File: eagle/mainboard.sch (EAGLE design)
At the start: 50 parts

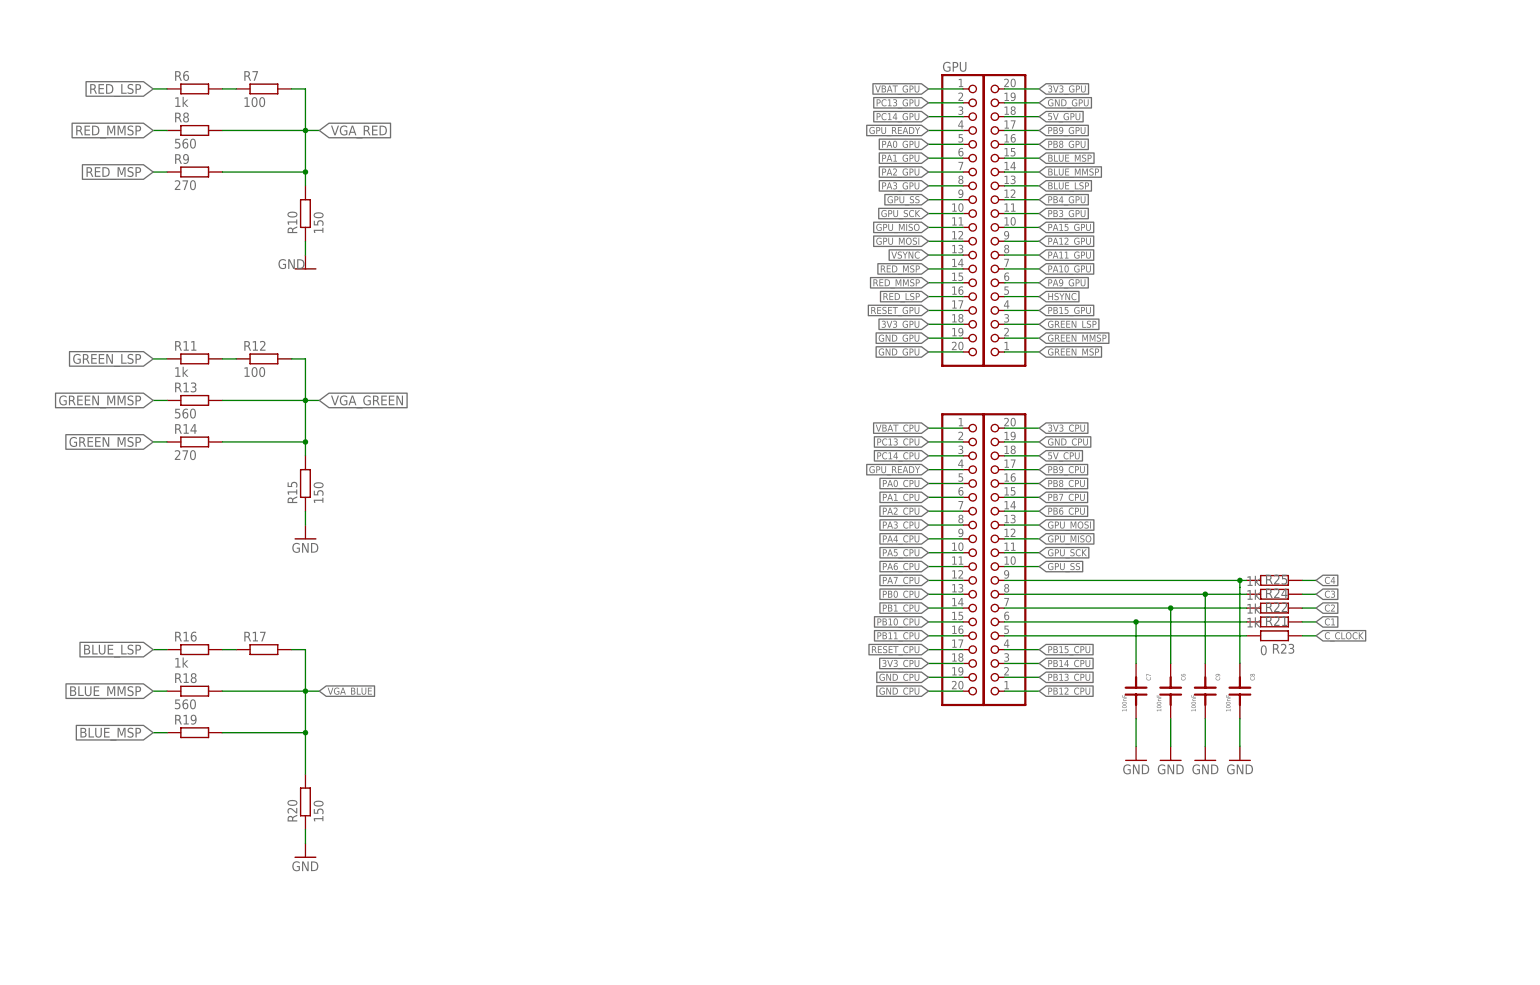
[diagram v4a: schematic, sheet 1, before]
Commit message: changed connector library ad wired up to cpu/gpu
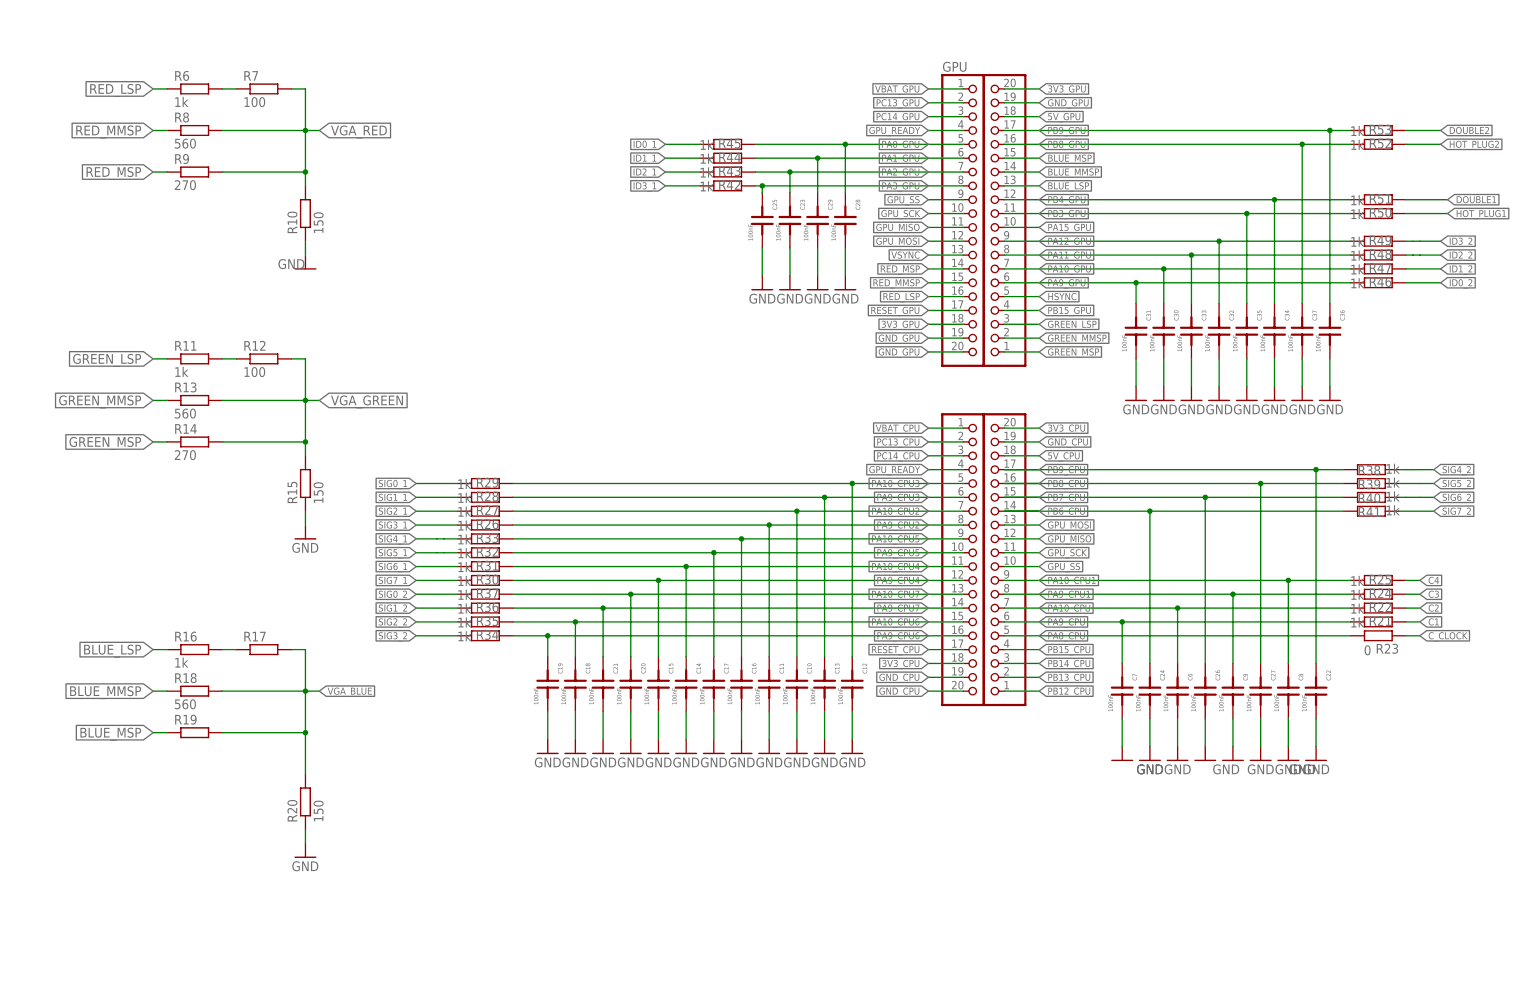
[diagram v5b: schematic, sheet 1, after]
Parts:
- added C10, C11, C12, C13, C14, C15, C16, C17, C18, C19, C20, C21, C22, C23, C24, C25, C26, C27, C28, C29, C30, C31, C32, C33, C34, C35, C36, C37: 100nF, deto:C1
- added R26, R27, R28, R29, R30, R31, R32, R33, R34, R35, R36, R37, R38, R39, R40, R41, R42, R43, R44, R45, R46, R47, R48, R49, R50, R51, R52, R53: 1k, rcl:R-EU_R0805
- added U$2: 3511220BMSS0BNA1_2.54MM_2X20_MALE, BtoB_connector:3511220BMSS0BNA1_2.54MM_2X20_MALE
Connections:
- removed net PA0_CPU: CPU2.5
- removed net PA1_CPU: CPU2.6
- removed net PA2_CPU: CPU2.7
- removed net PA3_CPU: CPU2.8
- removed net PA4_CPU: CPU2.9
- removed net PA5_CPU: CPU2.10
- removed net PA6_CPU: CPU2.11
- removed net PA7_CPU: CPU2.12
- removed net PB0_CPU: CPU2.13
- removed net PB10_CPU: CPU2.15
- removed net PB11_CPU: CPU2.16
- removed net PB1_CPU: CPU2.14
- new net DOUBLE1: R51.1, U$1.DOUBLE
- new net DOUBLE2: R53.1, U$2.DOUBLE
- new net HOT_PLUG1: R50.1, U$1.HOT_PLUG
- new net HOT_PLUG2: R52.1, U$2.HOT_PLUG
- new net ID0_1: R45.2, U$1.ID0
- new net ID0_2: R46.1, U$2.ID0
- new net ID1_1: R44.2, U$1.ID1
- new net ID1_2: R47.1, U$2.ID1
- new net ID2_1: R43.2, U$1.ID2
- new net ID2_2: R48.1, U$2.ID2
- new net ID3_1: R42.2, U$1.ID3
- new net ID3_2: R49.1, U$2.ID3
- new net PA10_CPU2: C10.2, CPU2.7, R27.1
- new net PA10_CPU3: C12.2, CPU2.5, R29.1
- new net PA10_CPU4: C14.2, CPU2.11, R31.1
- new net PA10_CPU5: C16.2, CPU2.9, R33.1
- new net PA10_CPU6: C18.2, CPU2.15, R35.1
- new net PA10_CPU7: C20.2, CPU2.13, R37.1
- new net PA9_CPU2: C11.2, CPU2.8, R26.1
- new net PA9_CPU3: C13.2, CPU2.6, R28.1
- new net PA9_CPU4: C15.2, CPU2.12, R30.1
- new net PA9_CPU5: C17.2, CPU2.10, R32.1
- new net PA9_CPU6: C19.2, CPU2.16, R34.1
- new net PA9_CPU7: C21.2, CPU2.14, R36.1
- new net SIG0_1: R29.2, U$1.SIG0
- new net SIG0_2: R37.2, U$2.SIG0
- new net SIG1_1: R28.2, U$1.SIG1
- new net SIG1_2: R36.2, U$2.SIG1
- new net SIG2_1: R27.2, U$1.SIG2
- new net SIG2_2: R35.2, U$2.SIG2
- new net SIG3_1: R26.2, U$1.SIG3
- new net SIG3_2: R34.2, U$2.SIG3
- new net SIG4_1: R33.2, U$1.SIG4
- new net SIG4_2: R38.2, U$2.SIG4
- new net SIG5_1: R32.2, U$1.SIG5
- new net SIG5_2: R39.2, U$2.SIG5
- new net SIG6_1: R31.2, U$1.SIG6
- new net SIG6_2: R40.2, U$2.SIG6
- new net SIG7_1: R30.2, U$1.SIG7
- new net SIG7_2: R41.2, U$2.SIG7
- net 3V3_CPU: now also U$1.3V3, U$2.3V3
- net 5V_CPU: now also U$1.5V, U$2.5V
- net GND: now also C10.1, C11.1, C12.1, C13.1, C14.1, C15.1, C16.1, C17.1, C18.1, C19.1, C20.1, C21.1, C22.1, C23.1, C24.1, C25.1, C26.1, C27.1, C28.1, C29.1, C30.1, C31.1, C32.1, C33.1, C34.1, C35.1, C36.1, C37.1
- net GND_CPU: now also U$1.GND, U$2.GND
- net PA0_GPU: now also C28.2, R45.1
- net PA10_GPU: now also C30.2, R47.2
- net PA11_GPU: now also C33.2, R48.2
- net PA12_GPU: now also C32.2, R49.2
- net PA1_GPU: now also C29.2, R44.1
- net PA2_GPU: now also C23.2, R43.1
- net PA3_GPU: now also C25.2, R42.1
- net PA9_GPU: now also C31.2, R46.2
- net PB3_GPU: now also C35.2, R50.2
- net PB4_GPU: now also C34.2, R51.2
- net PB6_CPU: now also C24.2, R41.1
- net PB7_CPU: now also C26.2, R40.1
- net PB8_CPU: now also C27.2, R39.1
- net PB8_GPU: now also C37.2, R52.2
- net PB9_CPU: now also C22.2, R38.1
- net PB9_GPU: now also C36.2, R53.2
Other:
- moved on the sheet: C6, C7, C8, C9, R21, R22, R23, R24, R25, U$1

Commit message: wired sd card slot
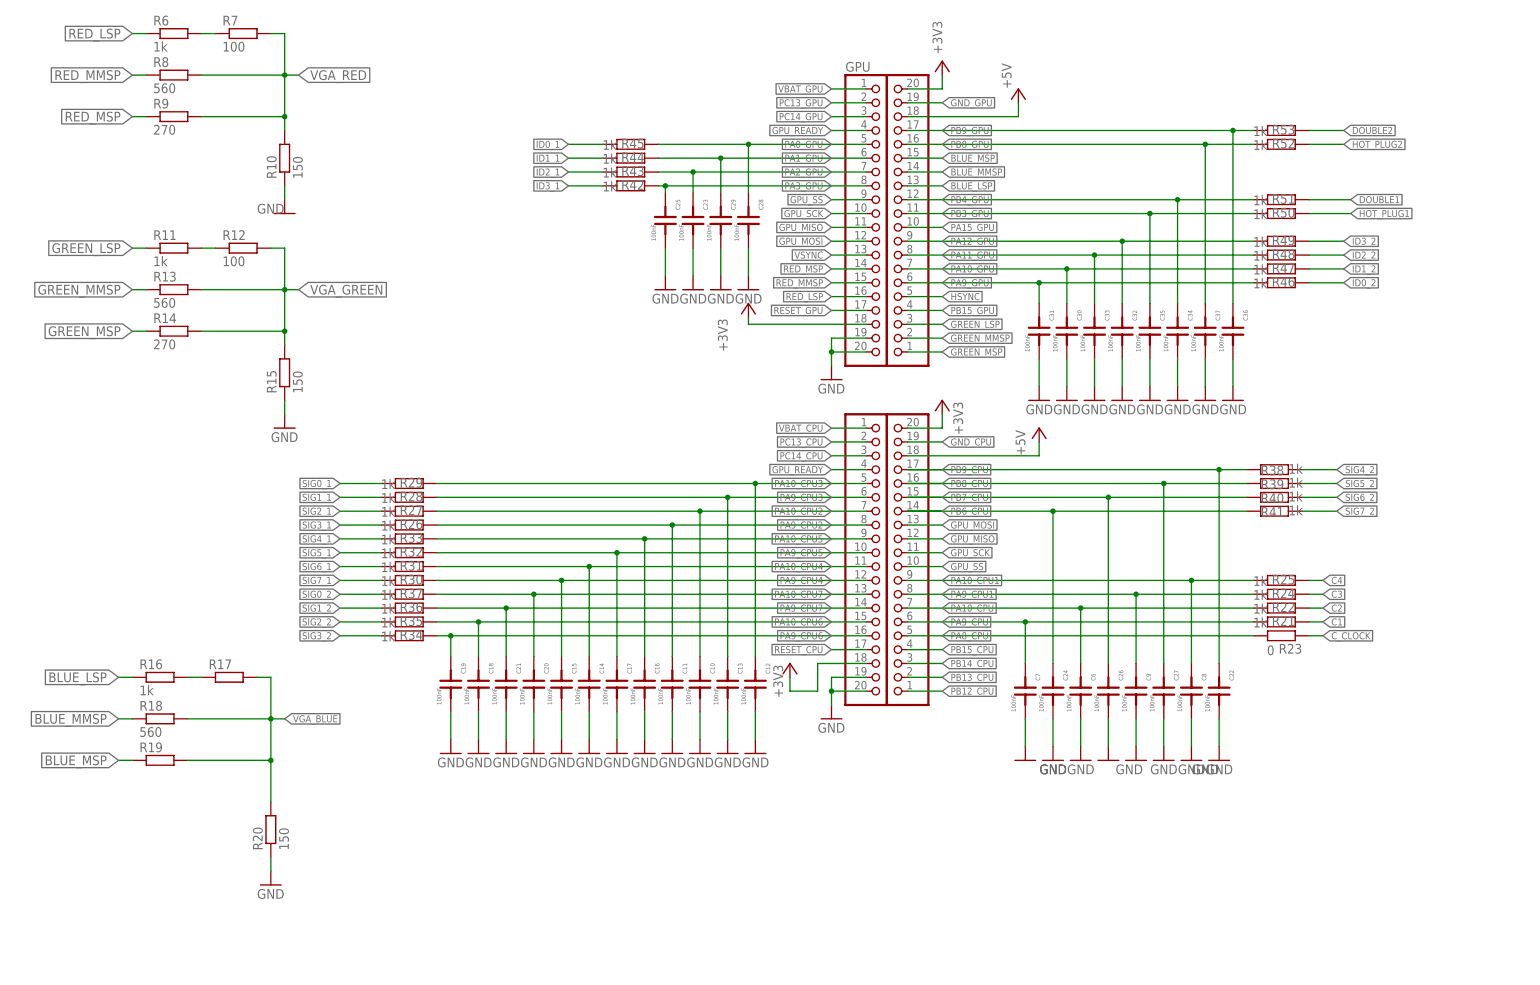
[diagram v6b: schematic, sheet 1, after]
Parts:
- added J1: SD_CARD_SOCKET, sd_card_sparkfun:SD_CARD_SOCKET
- added R54, R56: 10k, rcl:R-EU_R0805
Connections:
- removed net 3V3_GPU: GPU.18, GPU1.20
- removed net 5V_GPU: GPU1.18
- new net +3V3: CPU.20, CPU2.18, GPU.18, GPU1.20, J1.VDD, R54.2, R56.2
- net +5V: now also CPU.18, GPU1.18
- net 3V3_CPU: no longer CPU.20, CPU2.18
- net 5V_CPU: no longer CPU.18
- net GND: now also CPU2.19, CPU2.20, GPU.19, GPU.20, J1.SH@1, J1.SH@2, J1.VSS1, J1.VSS2
- net GND_CPU: no longer CPU2.19, CPU2.20
- net GND_GPU: no longer GPU.19, GPU.20
- net PB12_CPU: now also J1.CD/DAT3
- net PB13_CPU: now also J1.CLK
- net PB14_CPU: now also J1.DAT0, R56.1
- net PB15_CPU: now also J1.CMD
- net PC14_CPU: now also J1.CD, R54.1
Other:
- moved on the sheet: C10, C11, C12, C13, C14, C15, C16, C17, C18, C19, C20, C21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

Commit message: finalized schematik with detommaso and spiss supervision
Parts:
- removed C10, C11, C12, C13, C14, C15, C16, C17, C18, C19, C20, C21, C6, C7, C8, C9: 100nF, deto:C1
- added R55, R57, R58, R59, R60: (no value), rcl:R-EU_R0805
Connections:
- new net N$11: R57.2, USB-CONTROLLER1.CC
- new net N$12: R58.2, USB-CONTROLLER4.CC
- new net N$13: R59.2, USB-CONTROLLER3.CC
- new net N$14: R60.2, USB-CONTROLLER2.CC
- new net N$8: POWER-IN.CC, R55.2
- net +3V3: now also R55.1, R57.1, R58.1, R59.1, R60.1
- net GND: no longer C10.1, C11.1, C12.1, C13.1, C14.1, C15.1, C16.1, C17.1, C18.1, C19.1, C20.1, C21.1, C6.1, C7.1, C8.1, C9.1, POWER-IN.CC, USB-CONTROLLER1.CC, USB-CONTROLLER2.CC, USB-CONTROLLER3.CC, USB-CONTROLLER4.CC
- net PA10_CPU: no longer C6.2
- net PA10_CPU1: no longer C8.2
- net PA10_CPU2: no longer C10.2
- net PA10_CPU3: no longer C12.2
- net PA10_CPU4: no longer C14.2
- net PA10_CPU5: no longer C16.2
- net PA10_CPU6: no longer C18.2
- net PA10_CPU7: no longer C20.2
- net PA9_CPU: no longer C7.2
- net PA9_CPU1: no longer C9.2
- net PA9_CPU2: no longer C11.2
- net PA9_CPU3: no longer C13.2
- net PA9_CPU4: no longer C15.2
- net PA9_CPU5: no longer C17.2
- net PA9_CPU6: no longer C19.2
- net PA9_CPU7: no longer C21.2
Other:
- moved on the sheet: C1, C2, R1, R16, R17, R18, R19, R2, R20, R26, R27, R28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

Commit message: Schematic V1
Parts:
- removed C22, C24, C26, C27: 100nF, deto:C1
- removed J1: SD_CARD_SOCKET, sd_card_sparkfun:SD_CARD_SOCKET
- added C6, C7: 100nF, deto:C1
- added CONTROLLER-IN: 632723100011_USBC_3.1, Eagle_WR-USB (rev22c):632723100011_USBC_3.1
- added IC1, IC4: 74HCT151D, 74xx-eu:74HCT151D
- added IC2: 74HC04D, 74xx-eu:74HC04D
- added IC7: 74HC590D, 74xx-eu:74HC590D
- added JP1, JP10, JP11, JP12, JP13, JP2, JP3, JP9: (no value), pinhead:PINHD-1X2
- added JP14: (no value), pinhead:PINHD-1X1
- added JP15: (no value), pinhead:PINHD-1X4
- added R61, R62, R63, R64, R65, R66, R67, R68: 10k, rcl:R-EU_R0805
- added R70: 5k1Ω, rcl:R-EU_R0805
- added R71: 0Ω, rcl:R-EU_R0805
- added SD-CARD: SD_CARD_SOCKET, sd_card_sparkfun:SD_CARD_SOCKET
- R1, R2, R3, R4, R5: value Ferrit -> 0Ω; device deto:R2 -> rcl:R-EU_R0805
- R55: value (none) -> 5k1Ω
- R57, R58, R59, R60: value (none) -> 56kΩ
- renumbered U$1 to EXTENSION1, U$2 to EXTENSION2
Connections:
- removed net 3V3_CPU: EXTENSION1.3V3, EXTENSION2.3V3
- removed net 5V_CPU: EXTENSION1.5V, EXTENSION2.5V
- removed net GND_CPU: CPU.19, EXTENSION1.GND, EXTENSION2.GND
- removed net GND_GPU: GPU1.19
- new net A: IC4A.D7, JP9.2, R64.1
- new net B: IC4A.D6
- new net CLOCK: CONTROLLER-IN.DN1, IC7A.CLK, IC7A.RCK, JP14.1
- new net CONTROLLER_OUT: CONTROLLER-IN.DP1, IC1A.Y, IC4A.Y
- new net DOWN: IC4A.D2
- new net LEFT: IC4A.D1
- new net N$11: R61.2, R62.2, R63.2, R64.2, R65.2, R66.2, R67.2, R68.2
- new net N$15: JP1.2, R61.1
- new net N$17: JP2.2, R62.1
- new net N$19: JP3.2, R63.1
- new net N$20: JP13.2, R65.1
- new net N$22: JP12.2, R66.1
- new net N$23: JP11.2, R67.1
- new net N$24: IC1A.C, IC4A.A, IC7A.QA, JP15.1
- new net N$25: IC1A.B, IC4A.B, IC7A.QB, JP15.2
- new net N$26: IC1A.A, IC4A.C, IC7A.QC, JP15.3
- new net N$27: IC1A.G, IC2A.I, IC7A.QD, JP15.4
- new net N$28: IC1A.W
- new net N$29: IC2A.O, IC4A.G
- new net N$32: CONTROLLER-IN.VBUS, CONTROLLER-IN.VBUS1, R71.1
- new net N$33: CONTROLLER-IN.CC, R70.2
- new net RIGHT: IC4A.D0
- new net SELECT: IC4A.D4
- new net START: IC4A.D5
- new net UP: IC4A.D3, JP10.2, R68.1
- net +3V3: now also C6.2, EXTENSION1.3V3, EXTENSION2.3V3, IC1A.D7, SD-CARD.VDD; no longer J1.VDD, R55.1, R57.1, R58.1, R59.1, R60.1
- net +5V: now also C7.2, EXTENSION1.5V, EXTENSION2.5V, IC7A.CCLR, JP1.1, JP10.1, JP11.1, JP12.1, JP13.1, JP2.1, JP3.1, JP9.1, R57.1, R58.1, R59.1, R60.1, R71.2
- net GND: now also C6.1, C7.1, CONTROLLER-IN.GND, CONTROLLER-IN.GND1, CONTROLLER-IN.SBU1, CONTROLLER-IN.SHIELD, CONTROLLER-IN.SHIELD1, CONTROLLER-IN.SSRXN2, CONTROLLER-IN.SSRXP2, CONTROLLER-IN.SSTXN1, CONTROLLER-IN.SSTXP1, CPU.19, EXTENSION1.GND, EXTENSION2.GND, GPU1.19, IC1A.D0, IC1A.D1, IC1A.D2, IC1A.D3, IC1A.D4, IC1A.D5, IC1A.D6, IC2B.I, IC2C.I, IC2D.I, IC2E.I, IC2F.I, IC7A.CCKEN, IC7A.G, R55.1, R70.1, SD-CARD.SH@1, SD-CARD.SH@2, SD-CARD.VSS1, SD-CARD.VSS2, VGA.11; no longer C22.1, C24.1, C26.1, C27.1, J1.SH@1, J1.SH@2, J1.VSS1, J1.VSS2
- net ID0_2: now also R49.1; no longer R46.1
- net ID1_2: now also R48.1; no longer R47.1
- net ID2_2: now also R47.1; no longer R48.1
- net ID3_2: now also R46.1; no longer R49.1
- net N$4: now also R4.1; no longer R3.1
- net N$5: now also R3.1; no longer R4.1
- net PB12_CPU: now also SD-CARD.CD/DAT3; no longer J1.CD/DAT3
- net PB13_CPU: now also SD-CARD.CLK; no longer J1.CLK
- net PB14_CPU: now also SD-CARD.DAT0; no longer J1.DAT0
- net PB15_CPU: now also SD-CARD.CMD; no longer J1.CMD
- net PB6_CPU: no longer C24.2
- net PB7_CPU: no longer C26.2
- net PB8_CPU: no longer C27.2
- net PB9_CPU: no longer C22.2
- net PC14_CPU: now also SD-CARD.CD; no longer J1.CD
- net VGA_BLUE: now also VGA.3; no longer VGA.2
- net VGA_GREEN: now also VGA.2
- net VGA_RED: no longer VGA.3
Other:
- moved on the sheet: C1, C2, C3, C4, C5, JP4, JP5, JP6, JP7, JP8, R1, R2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
